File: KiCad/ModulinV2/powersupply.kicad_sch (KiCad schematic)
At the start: 43 parts, among them IC27 NCP5500DADJR2G, IC28 NCP5500DADJR2G, IC29 NCP5500DADJR2G, IC30 NCP5500DADJR2G, IC31 LM2576S-12_NOPB, IC32 LM2576S-12_NOPB, J4 PJ-002B

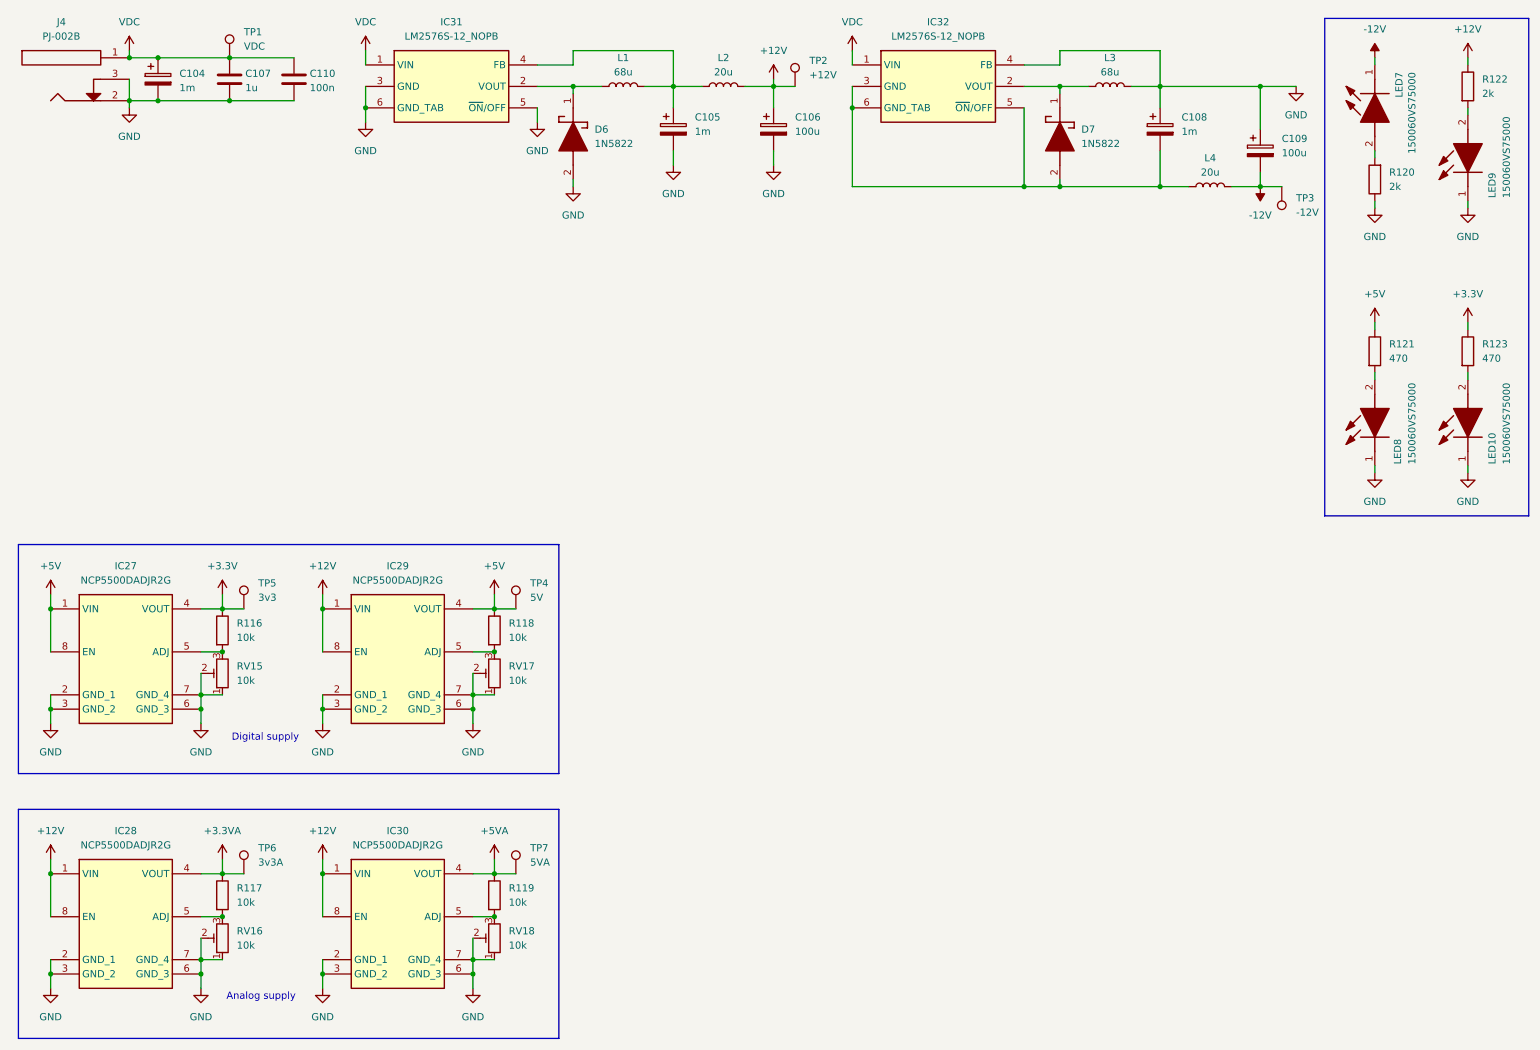
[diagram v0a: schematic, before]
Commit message: Revert "Modified selection LED schematic and supply caps"
This reverts commit f7ca9d31056dcb2cadf4048ae59e1f5625a2aefa.
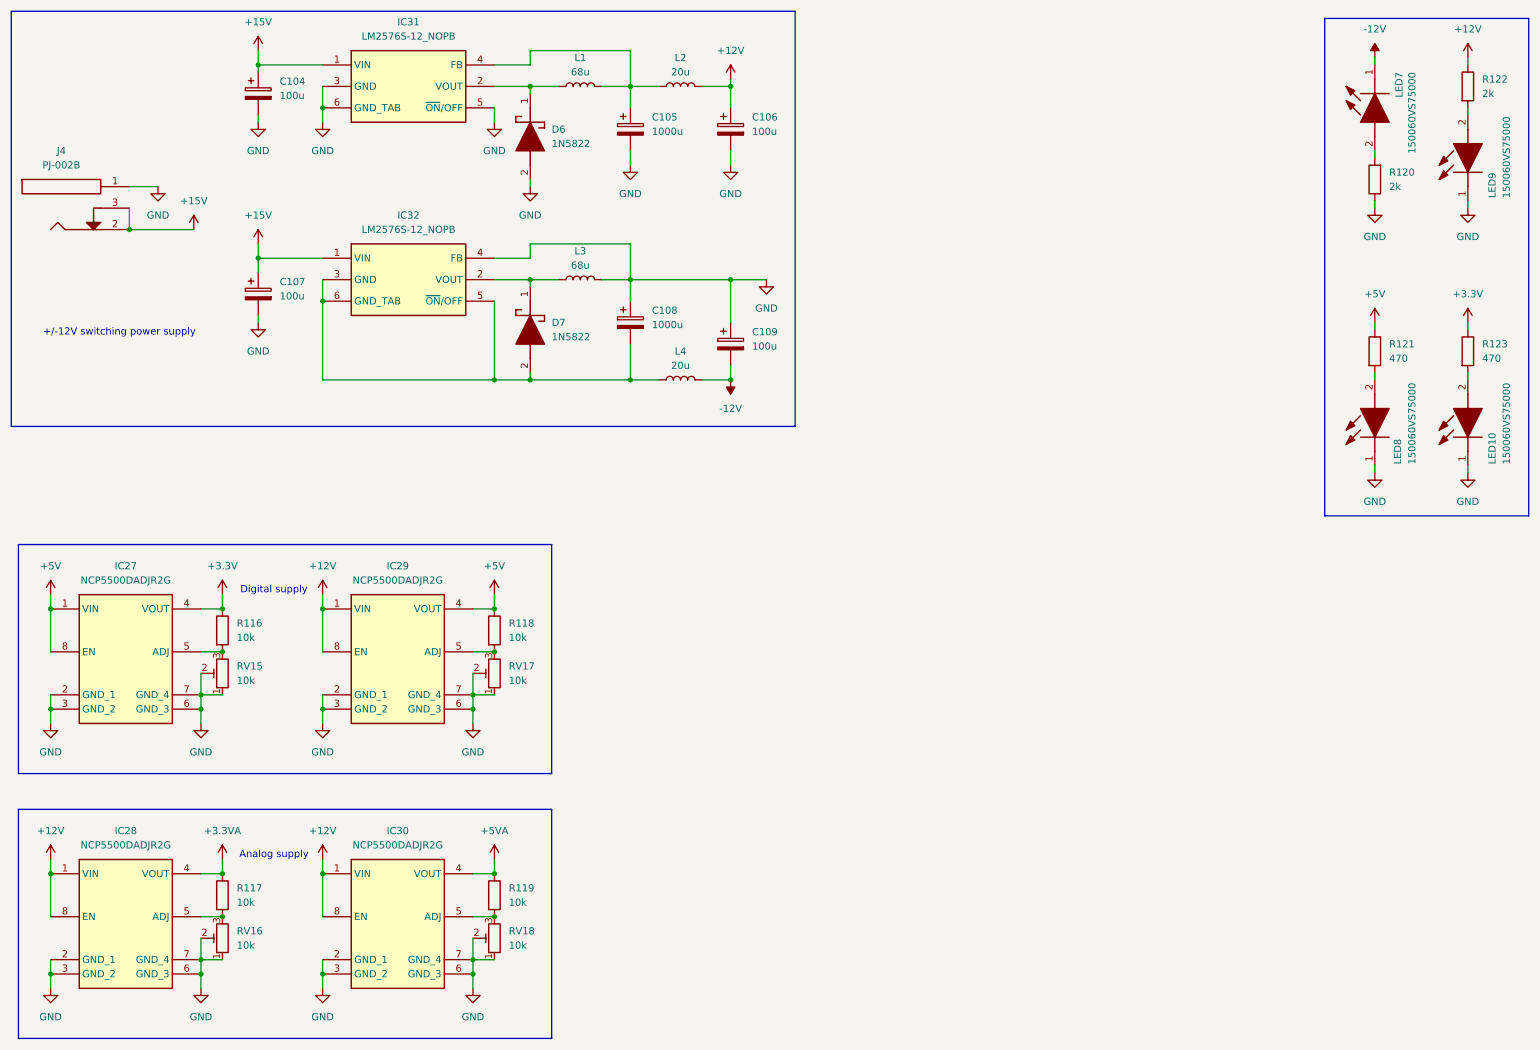
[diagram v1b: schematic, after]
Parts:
- removed C107: 1u, symbol Device:C
- removed C110: 100n, symbol Device:C
- removed TP1: VDC, symbol Connector:TestPoint
- removed TP2: +12V, symbol Connector:TestPoint
- removed TP3: -12V, symbol Connector:TestPoint
- removed TP4: 5V, symbol Connector:TestPoint
- removed TP5: 3v3, symbol Connector:TestPoint
- removed TP6: 3v3A, symbol Connector:TestPoint
- removed TP7: 5VA, symbol Connector:TestPoint
- added C107: 100u, symbol Device:C_Polarized
- C104: value 1m -> 100u
- C105, C108: value 1m -> 1000u
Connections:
- net GND: now also J4.1, C107.2; no longer J4.2, J4.3
- net VDC renamed +15V
- net +15V: now also J4.2, J4.3, C107.1; no longer J4.1
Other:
- note added: "+/-12V switching power supply"
- moved on the sheet: C104, C105, C106, C108, C109, D6, D7, IC31, IC32, J4, L1, L2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
